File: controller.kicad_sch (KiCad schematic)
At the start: 15 parts, among them U4 STM32H742VGTx

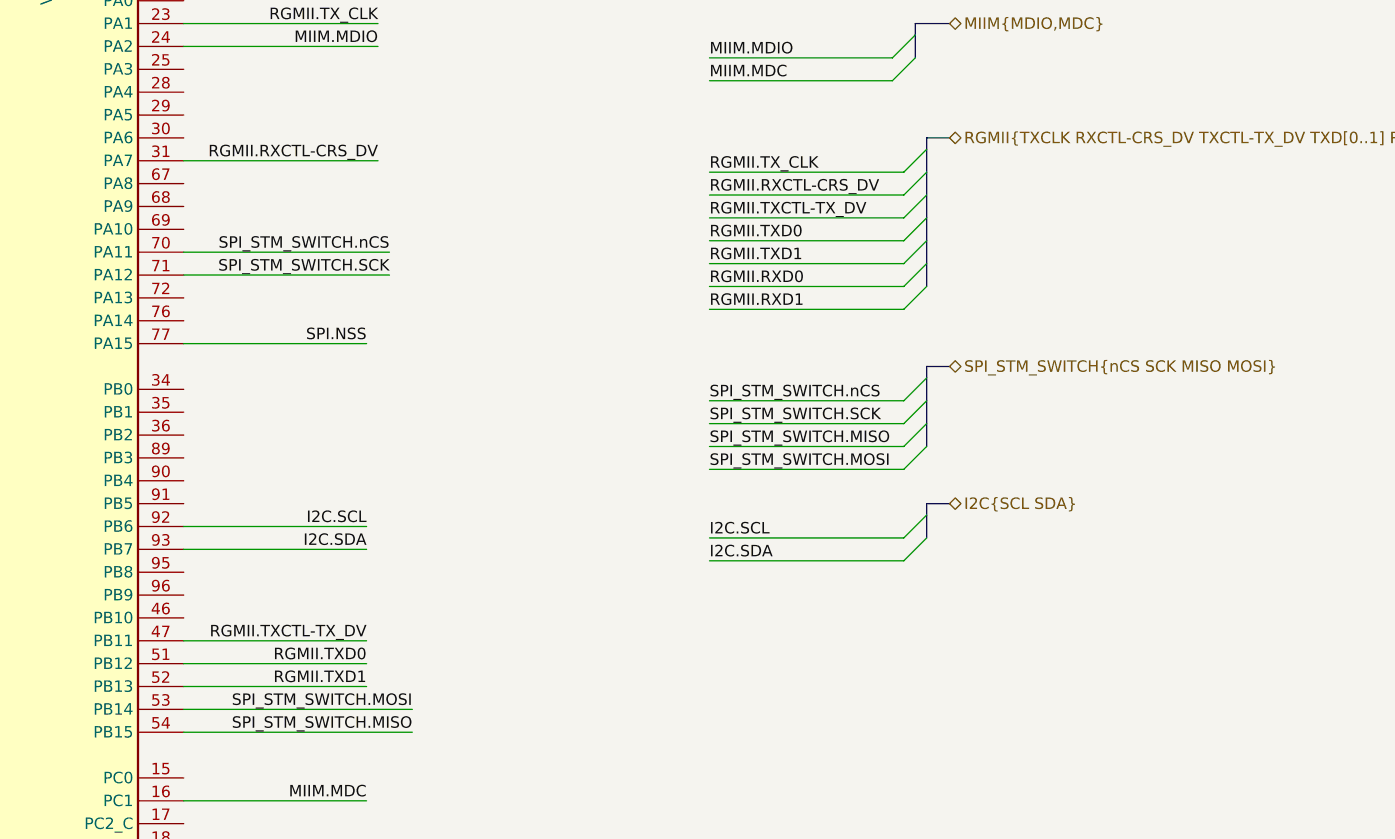
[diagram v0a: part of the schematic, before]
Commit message: adds uart support. Refs:#1
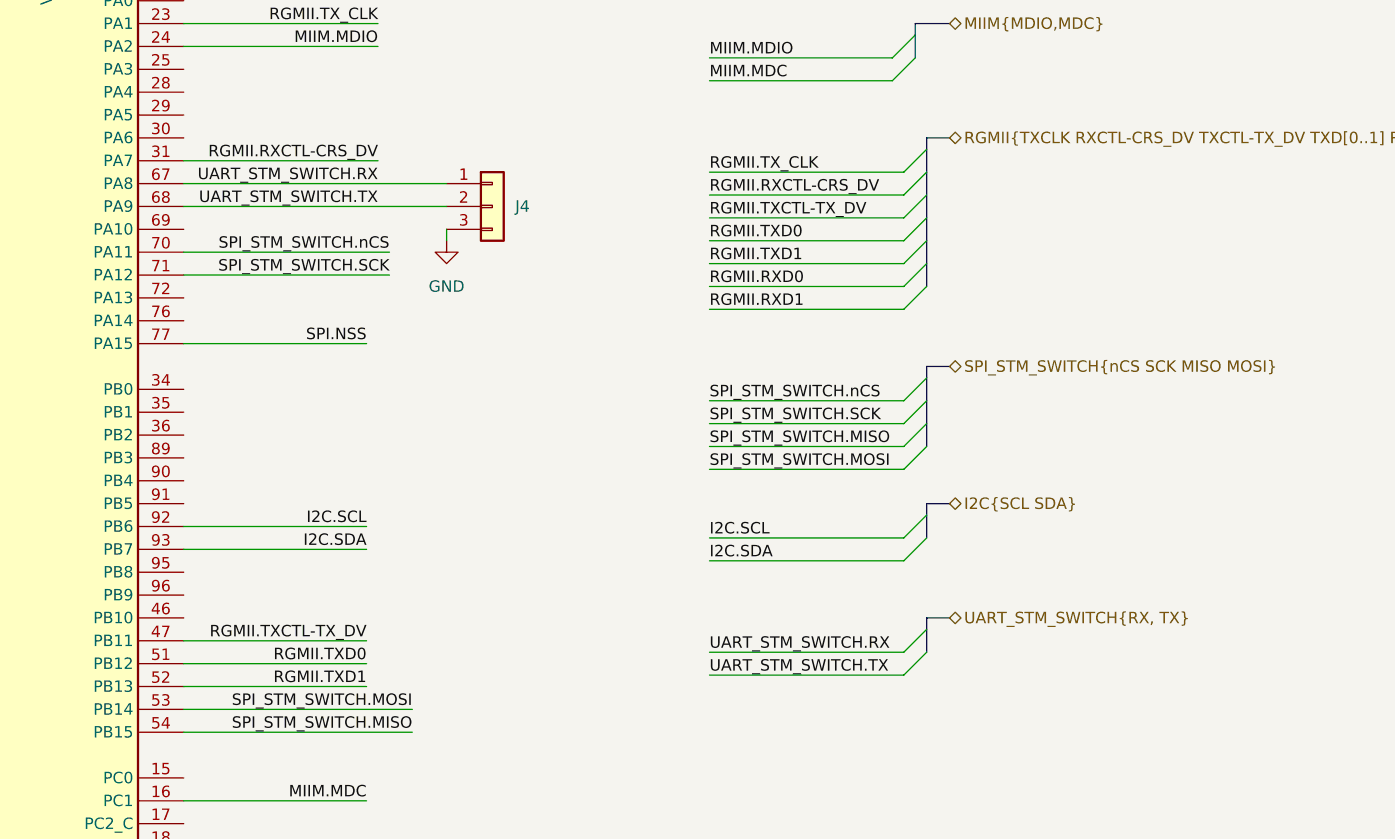
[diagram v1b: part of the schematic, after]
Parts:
- added J4: (no value), KL:03x01_2.54mm_Header, symbol KL_Headers:03x01_2.54mm_Header
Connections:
- net GND: now also J4.3 (Pin_3)
- net UART_STM_SWITCH.RX: now reaches U4.67 (PA8)
- net UART_STM_SWITCH.RX: now also J4.1 (Pin_1)
- net UART_STM_SWITCH.TX: now reaches U4.68 (PA9)
- net UART_STM_SWITCH.TX: now also J4.2 (Pin_2)

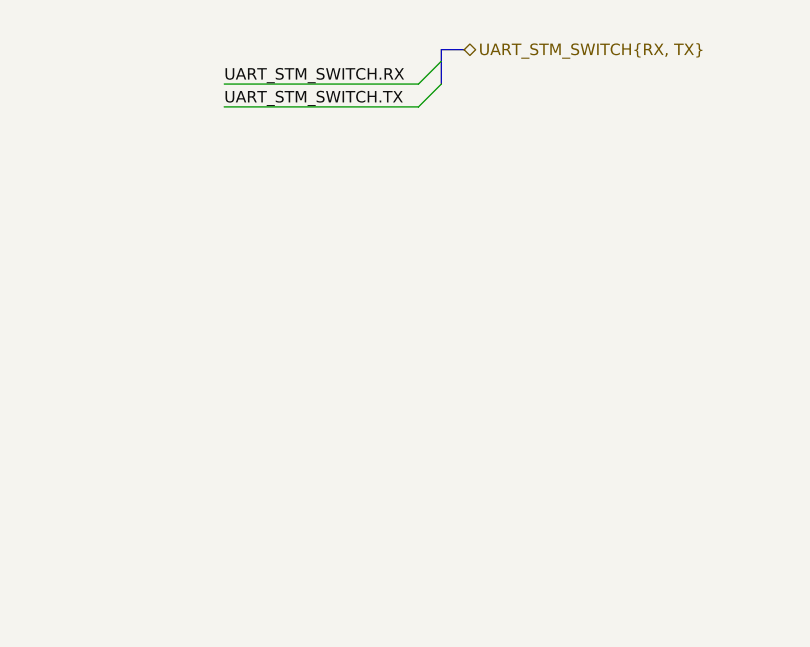
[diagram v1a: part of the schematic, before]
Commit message: initial commit for jtag header. WIP. Refs: #1
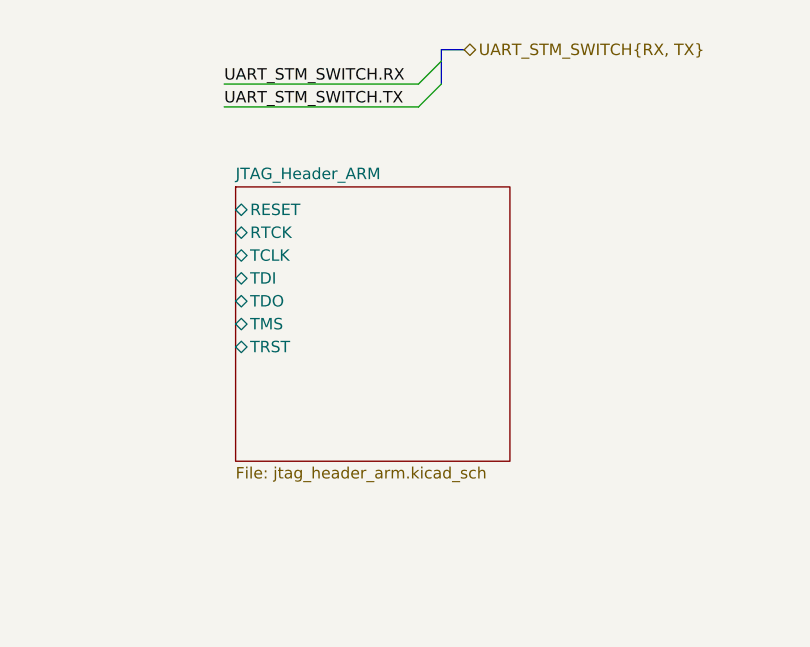
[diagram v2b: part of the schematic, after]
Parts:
- J4: value (none) -> ~
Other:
- added sheet JTAG_Header_ARM (jtag_header_arm.kicad_sch)
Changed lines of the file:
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@@
 			)
 		)
-		(property "Value" ""
+		(property "Value" "~"
 			(at 158.75 66.04 0)
 			(effects
@@
 				)
 			)
+		)
+	)
+	(sheet
+		(at 184.15 128.27)
+		(size 30.48 30.48)
+		(exclude_from_sim no)
+		(in_bom yes)
+		(on_board yes)
+		(dnp no)
+		(fields_autoplaced yes)
+		(stroke
+			(width 0.1524)
+			(type solid)
+		)
+		(fill
+			(color 0 0 0 0.0000)
+		)
+		(property "Sheetname" "JTAG_Header_ARM"
+			(at 184.15 127.5584 0)
+			(effects
+				(font
+					(size 1.27 1.27)
+				)
+				(justify left bottom)
+			)
+		)
+		(property "Sheetfile" "jtag_header_arm.kicad_sch"
+			(at 184.15 159.3346 0)
+			(effects
+				(font
+					(size 1.27 1.27)
+				)
+				(justify left top)
+			)
+		)
+		(pin "RESET" bidirectional
+			(at 184.15 130.81 180)
+			(effects
+				(font
+					(size 1.27 1.27)
+				)
+				(justify left)
+			)
+		)
+		(pin "RTCK" bidirectional
+			(at 184.15 133.35 180)
+			(effects
+				(font
+					(size 1.27 1.27)
+				)
+				(justify left)
+			)
+		)
+		(pin "TCLK" bidirectional
+			(at 184.15 135.89 180)
+			(effects
+				(font
+					(size 1.27 1.27)
+				)
+				(justify left)
+			)
+		)
+		(pin "TDI" bidirectional
+			(at 184.15 138.43 180)
+			(effects
+				(font
+					(size 1.27 1.27)
+				)
+				(justify left)
+			)
+		)
+		(pin "TDO" bidirectional
+			(at 184.15 140.97 180)
+			(effects
+				(font
+					(size 1.27 1.27)
+				)
+				(justify left)
+			)
+		)
+		(pin "TMS" bidirectional
+			(at 184.15 143.51 180)
+			(effects
+				(font
+					(size 1.27 1.27)
+				)
+				(justify left)
+			)
+		)
+		(pin "TRST" bidirectional
+			(at 184.15 146.05 180)
+			(effects
+				(font
+					(size 1.27 1.27)
+				)
+				(justify left)
+			)
+		)
+		(instances
+			(project "shish-lan"
+				(path "/d4536448-b109-4159-96e2-3dc21baf2d6e/06488c82-a47f-4277-b0ee-3bd211d8922a"
+					(page "17")
+				)
+			)

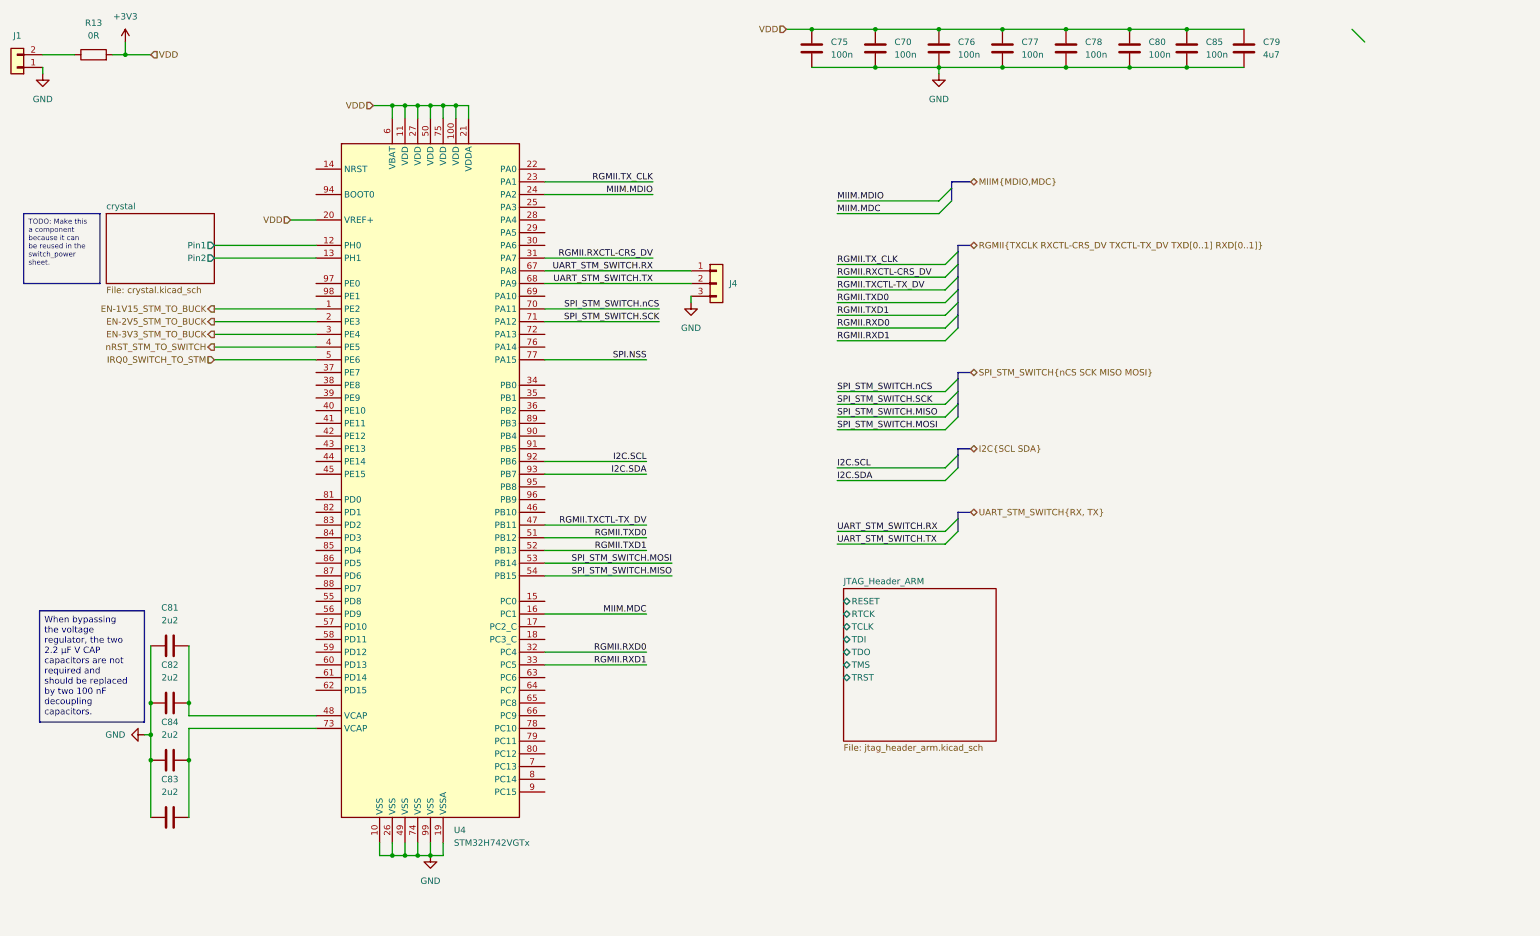
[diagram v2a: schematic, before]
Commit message: adds boot0 configuration header. Refs: #1
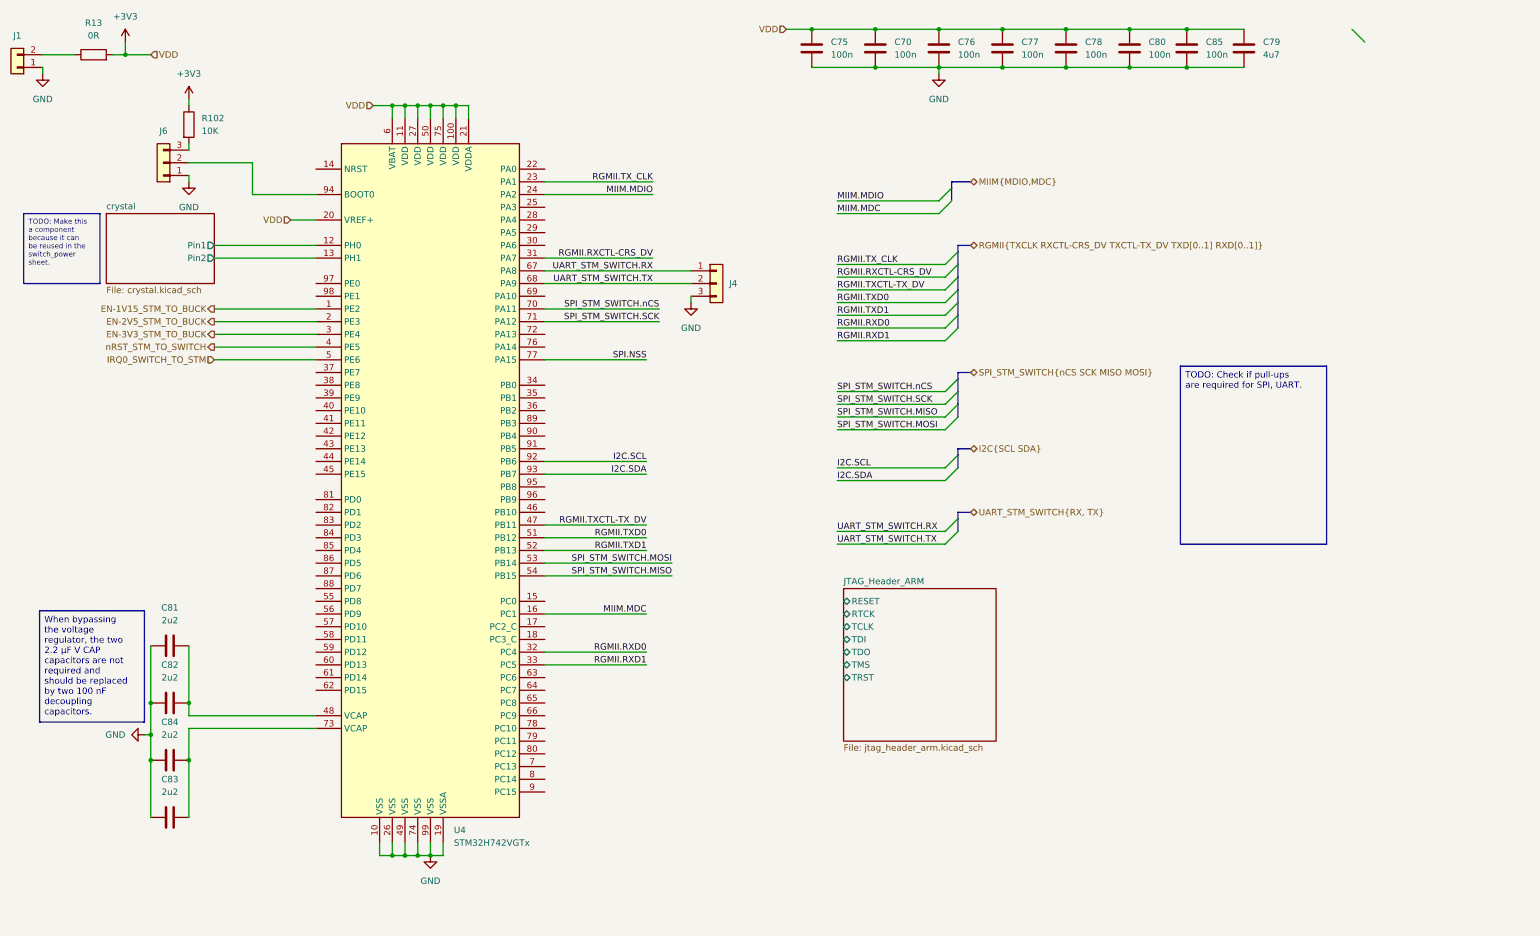
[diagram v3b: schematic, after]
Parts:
- added J6: ~, KL:03x01_2.54mm_Header, symbol KL_Headers:03x01_2.54mm_Header
- added R102: 10K, KL_Footprints:C_0603, symbol KL_R:R_10K_100mW_5_0603
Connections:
- net +3V3: now also R102.1
- net GND: now also J6.1 (Pin_1)
- net at U4.94 (BOOT0): now also J6.2 (Pin_2)
- new net: J6.3 (Pin_3), R102.2

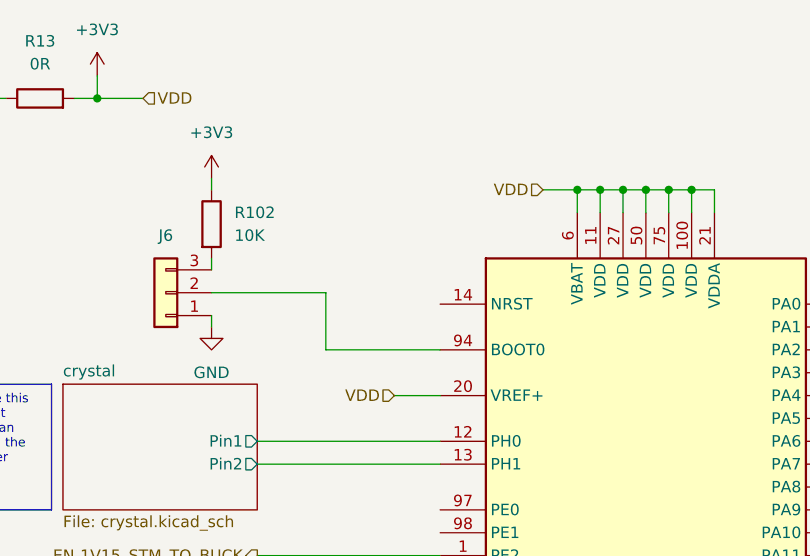
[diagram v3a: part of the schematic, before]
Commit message: adds testpoint to nrst pin for easier accessibility. Refs: #1
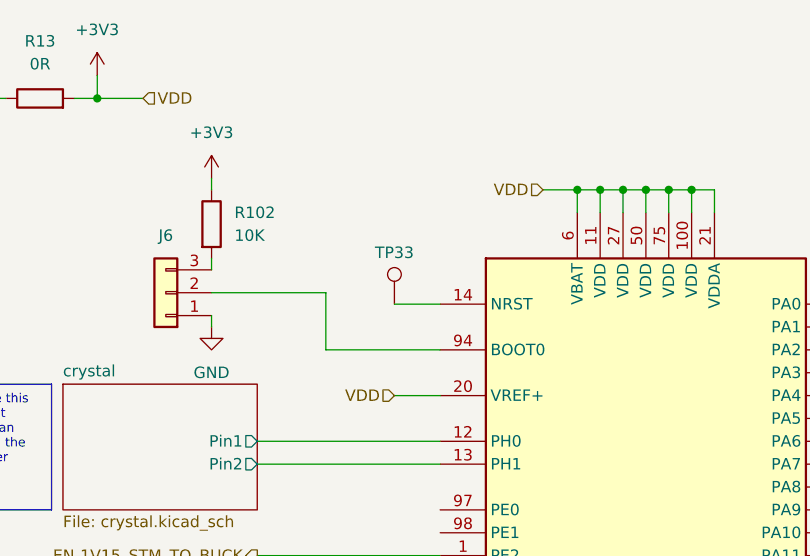
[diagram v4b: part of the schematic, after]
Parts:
- added TP33: ~, Connector_PinHeader_2.54mm:PinHeader_1x01_P2.54mm_Vertical, symbol KL_TP:TestPoint
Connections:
- net at U4.14 (NRST): now also TP33.1
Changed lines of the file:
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@@
+	(wire
+		(pts
+			(xy 73.66 44.45) (xy 78.74 44.45)
+		)
+		(stroke
+			(width 0)
+			(type default)
+		)
+	)
 	(wire
 		(pts
@@
 					(unit 1)
 				)
+			)
+		)
+	)
+	(symbol
+		(lib_id "KL_TP:TestPoint")
+		(at 73.66 44.45 0)
+		(unit 1)
+		(exclude_from_sim no)
+		(in_bom yes)
+		(on_board yes)
+		(dnp no)
+		(fields_autoplaced yes)
+		(property "Reference" "TP33"
+			(at 73.66 38.735 0)
+			(do_not_autoplace yes)
+			(effects
+				(font
+					(size 1.27 1.27)
+				)
+			)
+		)
+		(property "Value" "~"
+			(at 73.66 39.37 0)
+			(effects
+				(font
+					(size 1.27 1.27)
+				)
+				(hide yes)
+			)
+		)
+		(property "Footprint" "Connector_PinHeader_2.54mm:PinHeader_1x01_P2.54mm_Vertical"
+			(at 78.74 44.45 0)
+			(effects
+				(font
+					(size 1.27 1.27)
+				)
+				(hide yes)
+			)
+		)
+		(property "Datasheet" "~"
+			(at 78.74 44.45 0)
+			(effects
+				(font
+					(size 1.27 1.27)
+				)
+				(hide yes)
+			)
+		)
+		(property "Description" "test point"
+			(at 73.66 44.45 0)
+			(effects
+				(font
+					(size 1.27 1.27)
+				)
+				(hide yes)
+			)
+		)
+		(pin "1"
+		)
+		(instances
+			(project ""
+				(path "/d4536448-b109-4159-96e2-3dc21baf2d6e/06488c82-a47f-4277-b0ee-3bd211d8922a"
+					(reference "TP33")
+					(unit 1)
+				)
